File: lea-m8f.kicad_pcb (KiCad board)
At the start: 2 copper layers, 27 parts, among them CON1 USB-MICRO-B, J1 RF_IN, J2 DB9, J3 PPS, J4 30.72, P1 CONN_01X08, U100 B200_GPSDO, U2 MAX232, U3 LEA-M8F, U4 NC7SZ125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

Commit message: update pcb
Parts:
- removed C4: 100nF, SMD_Packages:SMD-0805
- removed C5: 10uF, SMD_Packages:SMD-0805
- removed C6: 10nF, SMD_Packages:SMD-0805
- removed C7: 1uF, SMD_Packages:SMD-0805
- removed J2: DB9, Connect:DB9FD
- removed U7: LT1962, lea-m8f:MS8
- added D1: DIODESCH, SMD_Packages:SMD-0603, F.Cu at (209.2, 66.9)
- added D2: PPS, SMD_Packages:SMD-0603, F.Cu at (197.9, 103.1)
- added D3: VDD, SMD_Packages:SMD-0603, F.Cu at (197.9, 109.7)
- added D4: DIODESCH, SMD_Packages:SMD-0603, B.Cu at (188.8, 97.4)
- added D5: VUSB, SMD_Packages:SMD-0603, F.Cu at (197.9, 106.4)
- added R10: 510, Resistors_SMD:R_0603_HandSoldering, F.Cu at (193.8, 103.1)
- added R11: 510, Resistors_SMD:R_0603_HandSoldering, F.Cu at (193.8, 109.7)
- added R12: 510, Resistors_SMD:R_0603_HandSoldering, F.Cu at (193.8, 106.4)
- added R8: 0, Resistors_SMD:R_0805, B.Cu at (195.5, 73.5)
- added U1: NC7SZ125, lea-m8f:SC70, F.Cu at (194.1, 99.3)
- C1: value 1uF -> 10uF
- C2: value 1uF -> 10nF
- U2: value MAX232 -> LT1962; footprint Housings_SOIC:SOIC-16_3.9x9.9mm_Pitch1.27mm -> lea-m8f:MS8
- moved C2 21.7 mm to (182.8, 99.0)
- moved C1 19.7 mm to (182.8, 96.7), turned to 180 degrees
- moved U2 18.7 mm to (183.8, 101.1), turned to 270 degrees
- moved C3 13.5 mm to (182.7, 107.9), turned to 180 degrees
- moved R1 2.69 mm to (195.5, 69.8), turned to 270 degrees
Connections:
- C1 pad 1: Net-(C1-Pad1) -> /VDDUSB
- C1 pad 2: Net-(C1-Pad2) -> GND
- C2 pad 2: Net-(C2-Pad2) -> /VDDUSB
- C3 pad 1: VCC -> /5VUSB
- C3 pad 2: Net-(C3-Pad2) -> GND
- P1 pad 1: (no net) -> VCC
- P1 pad 4: /SB_N -> /RESET_N
- P1 pad 5: (no net) -> /SCL
- P1 pad 6: /SCL -> /SDA
- P1 pad 7: /SDA -> /VBKP
- R1 pad 1: /ISP_N -> /SB_N
- R1 pad 2: /SB_N -> /ISP_N
- R6 pad 1: Net-(R6-Pad1) -> Net-(CON1-Pad3)
- R7 pad 1: Net-(R7-Pad1) -> Net-(CON1-Pad2)
- U100 pad 8: VCC -> /VDD_B200
- U2 pad 1: Net-(C1-Pad1) -> /VDDUSB
- U2 pad 2: Net-(C3-Pad2) -> /VDDUSB
- U2 pad 3: Net-(C1-Pad2) -> Net-(C2-Pad1)
- U2 pad 4: Net-(C2-Pad1) -> GND
- U2 pad 5: Net-(C2-Pad2) -> /5VUSB
- U2 pad 7: Net-(J2-Pad1) -> (no net)
- U2 pad 8: (no net) -> /5VUSB
- U3 pad 10: (no net) -> /RESET_N
- U3 pad 11: (no net) -> /VBKP
- U3 pad 24: VCC -> /VDDUSB
- U6 pad 6: Net-(R6-Pad1) -> Net-(CON1-Pad3)
- U6 pad 7: Net-(R7-Pad1) -> Net-(CON1-Pad2)
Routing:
- net VCC: track 149.1 -> 3.31 mm, vias 7 -> 2
- net /VBKP: track 0.00 -> 48.8 mm, vias 0 -> 1
- net /RESET_N: track 0.00 -> 47.9 mm, vias 0 -> 1
- net /VDDUSB: track 0.00 -> 46.6 mm, vias 0 -> 4
- net /SB_N: track 54.0 -> 18.3 mm, vias 3 -> 1
- net /PPS_BUFF: track 80.3 -> 56.7 mm
- net Net-(CON1-Pad2): track 6.08 -> 23.5 mm
- net Net-(CON1-Pad3): track 6.48 -> 23.6 mm
- net Net-(J2-Pad1): track 15.5 -> 0.00 mm
- net Net-(J2-Pad3): track 15.3 -> 0.00 mm, vias 1 -> 0
- net Net-(J2-Pad2): track 13.6 -> 0.00 mm, vias 1 -> 0
- net GND: track 115.3 -> 102.7 mm, vias 25 -> 34
- net /M8F_PPS: track 5.95 -> 18.1 mm, vias 0 -> 2
- net Net-(R7-Pad1): track 12.0 -> 0.00 mm
- net Net-(R6-Pad1): track 11.6 -> 0.00 mm
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- added copper zone on F.Cu, net VCC
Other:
- board text added: "1PPS"
- board text added: "VDD"
- board text added: "VUSB"
- board text added: "opendigitalradio.org"

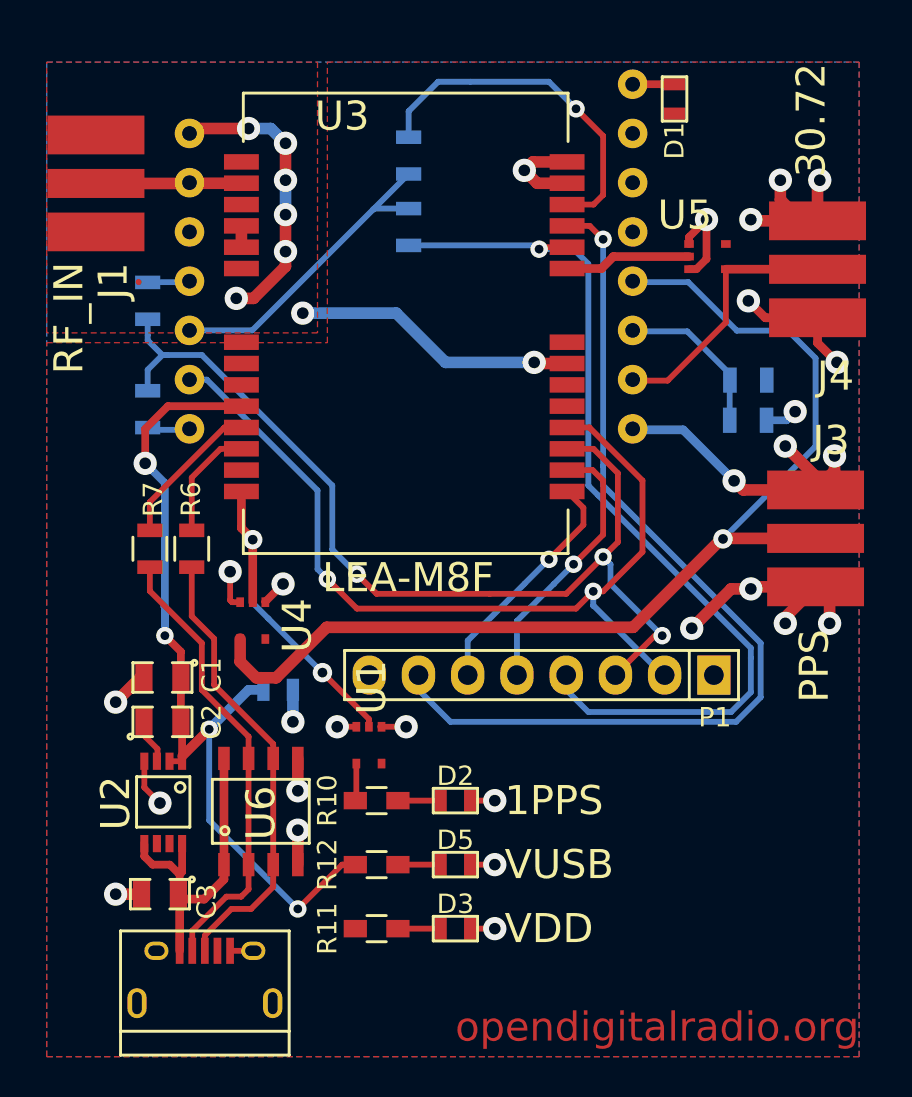
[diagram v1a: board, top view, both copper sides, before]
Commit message: Add text to PCB
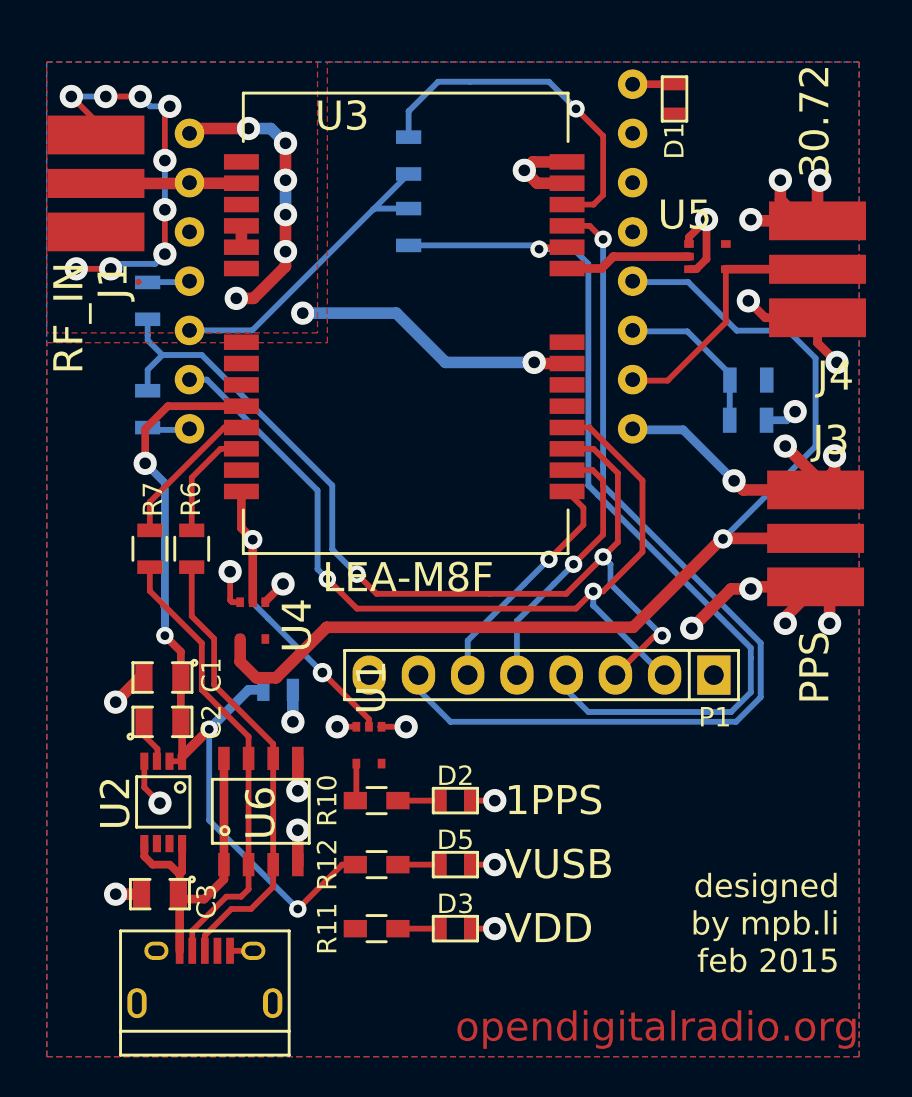
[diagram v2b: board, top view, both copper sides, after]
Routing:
- net GND: track 102.7 -> 123.2 mm, vias 34 -> 43
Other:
- board text added: "designed by mpb.li feb 2015"
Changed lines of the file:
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@@
     (links 95)
     (no_connects 0)
-    (area 0 0 0 0)
+    (area 175.646387 64.544615 219.2858 116.487901)
     (thickness 1.6)
-    (drawings 8)
-    (tracks 349)
+    (drawings 9)
+    (tracks 372)
     (zones 0)
     (modules 31)
@@
       (effects (font (size 1.5 1.5) (thickness 0.15)))
     )
-    (fp_text value PPS (at -0.0635 9.0805 90) (layer F.SilkS)
+    (fp_text value PPS (at -0.0381 9.1694 90) (layer F.SilkS)
       (effects (font (size 1.5 1.5) (thickness 0.15)))
     )
@@
       (effects (font (size 1.5 1.5) (thickness 0.15)))
     )
-    (fp_text value 30.72 (at -0.3302 -5.1943 90) (layer F.SilkS)
+    (fp_text value 30.72 (at -0.1397 -5.1435 90) (layer F.SilkS)
       (effects (font (size 1.5 1.5) (thickness 0.15)))
     )
@@
       (net 4 /5VUSB))
   )
+  (gr_text "designed\nby mpb.li\nfeb 2015" (at 217.7161 109.4359) (layer F.SilkS)
+    (effects (font (size 1.2 1.2) (thickness 0.2)) (justify right))
+  )
   (gr_line (start 176.8221 116.2939) (end 176.8221 64.9859) (angle 90) (layer Margin) (width 0.2))
   (gr_line (start 218.7321 116.2939) (end 176.8221 116.2939) (angle 90) (layer Margin) (width 0.2))
@@
   (via (at 215.4301 83.0199) (size 1.2) (layers F.Cu B.Cu) (net 2))
   (segment (start 214.9856 83.4644) (end 215.4301 83.0199) (width 0.4) (layer B.Cu) (net 2))
-  (segment (start 186.2801 110.8329) (end 187.4801 110.8329) (width 0.3) (layer F.Cu) (net 3) (status C00000))
+  (segment (start 179.3621 68.7489) (end 179.3621 68.0339) (width 0.3) (layer F.Cu) (net 3))
+  (segment (start 179.3621 68.0339) (end 178.0921 66.7639) (width 0.3) (layer F.Cu) (net 3))
+  (via (at 178.0921 66.7639) (size 1.2) (layers F.Cu B.Cu) (net 3))
+  (segment (start 178.0921 66.7639) (end 179.8701 66.7639) (width 0.3) (layer B.Cu) (net 3))
+  (via (at 179.8701 66.7639) (size 1.2) (layers F.Cu B.Cu) (net 3))
+  (segment (start 179.8701 66.7639) (end 181.6481 66.7639) (width 0.3) (layer F.Cu) (net 3))
+  (via (at 181.6481 66.7639) (size 1.2) (layers F.Cu B.Cu) (net 3))
+  (segment (start 181.6481 66.7639) (end 182.1561 67.2719) (width 0.3) (layer B.Cu) (net 3))
+  (segment (start 182.1561 67.2719) (end 183.1721 67.2719) (width 0.3) (layer B.Cu) (net 3))
+  (via (at 183.1721 67.2719) (size 1.2) (layers F.Cu B.Cu) (net 3))
+  (segment (start 183.1721 67.2719) (end 182.9181 67.5259) (width 0.3) (layer F.Cu) (net 3))
+  (segment (start 182.9181 67.5259) (end 182.9181 70.0659) (width 0.3) (layer F.Cu) (net 3))
+  (via (at 182.9181 70.0659) (size 1.2) (layers F.Cu B.Cu) (net 3))
+  (segment (start 182.9181 70.0659) (end 182.9181 72.6059) (width 0.3) (layer B.Cu) (net 3))
+  (via (at 182.9181 72.6059) (size 1.2) (layers F.Cu B.Cu) (net 3))
+  (segment (start 182.9181 72.6059) (end 182.9181 74.8919) (width 0.3) (layer F.Cu) (net 3))
+  (via (at 182.9181 74.8919) (size 1.2) (layers F.Cu B.Cu) (net 3))
+  (segment (start 182.9181 74.8919) (end 182.4101 75.3999) (width 0.3) (layer B.Cu) (net 3))
+  (segment (start 182.4101 75.3999) (end 180.3781 75.3999) (width 0.3) (layer B.Cu) (net 3))
+  (segment (start 180.3781 75.3999) (end 180.1241 75.6539) (width 0.3) (layer B.Cu) (net 3))
+  (via (at 180.1241 75.6539) (size 1.2) (layers F.Cu B.Cu) (net 3))
+  (segment (start 180.1241 75.6539) (end 178.3461 75.6539) (width 0.3) (layer F.Cu) (net 3))
+  (via (at 178.3461 75.6539) (size 1.2) (layers F.Cu B.Cu) (net 3))
+  (segment (start 186.2801 110.8329) (end 187.4801 110.8329) (width 0.3) (layer F.Cu) (net 3))
   (segment (start 198.6661 109.6899) (end 199.9361 109.6899) (width 0.3) (layer F.Cu) (net 3))
   (via (at 199.9361 109.6899) (size 1.2) (layers F.Cu B.Cu) (net 3))
@@
   )
   (zone (net 3) (net_name GND) (layer F.Cu) (hatch edge 0.508)
-    (connect_pads (clearance 0.3))
+    (connect_pads thru_hole_only (clearance 0.3))
     (min_thickness 0.254)
     (fill yes (arc_segments 16) (thermal_gap 0.4) (thermal_bridge_width 0.4))

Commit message: Correct LEA footprint, add silkscreen
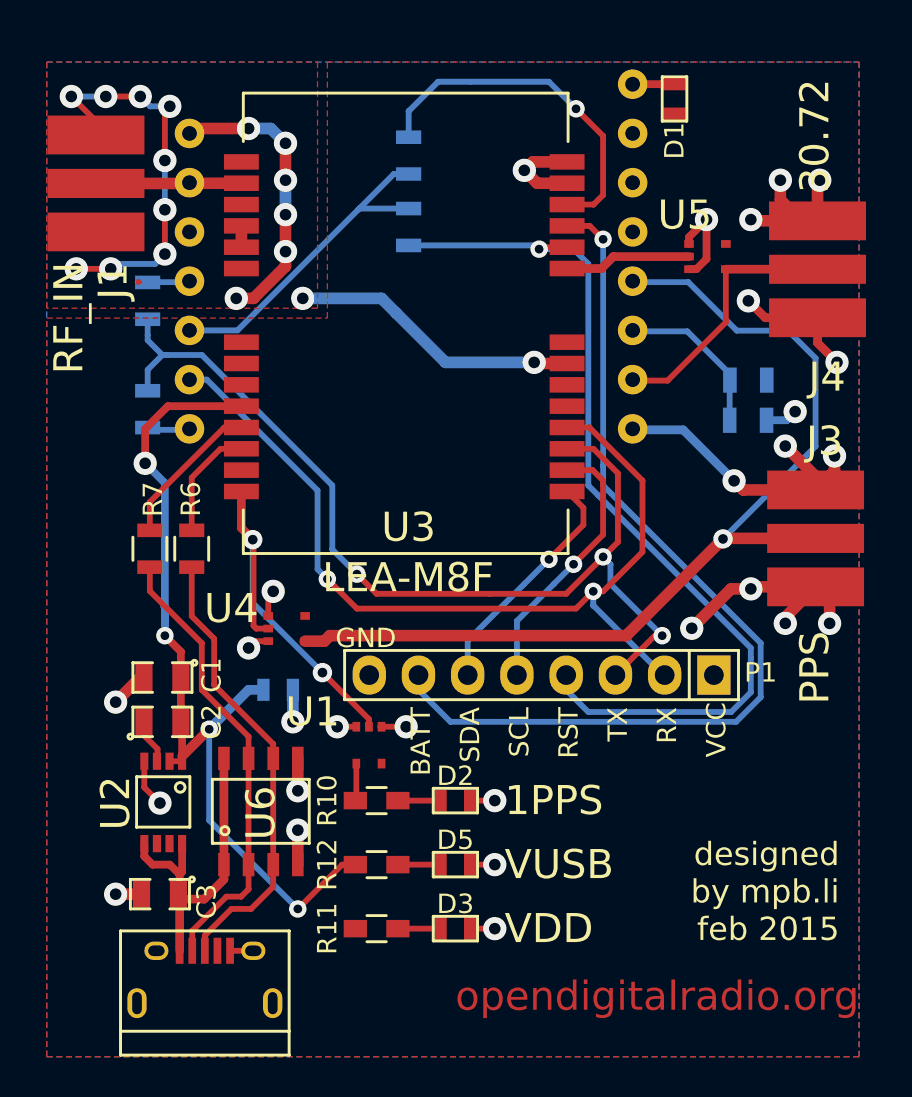
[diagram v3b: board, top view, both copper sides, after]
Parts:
- moved U4 0.73 mm to (188.3, 93.6), turned to 0 degrees
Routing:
- net /PPS_BUFF: track 56.7 -> 51.1 mm
- net /M8F_PPS: track 18.1 -> 20.2 mm
- net /ISP_N: track 17.2 -> 17.8 mm
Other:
- board text added: "BATT"
- board text added: "GND"
- board text added: "RST"
- board text added: "RX"
- board text added: "SCL"
- board text added: "SDA"
- board text added: "TX"
- board text added: "VCC"

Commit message: Fixed footprints and layout
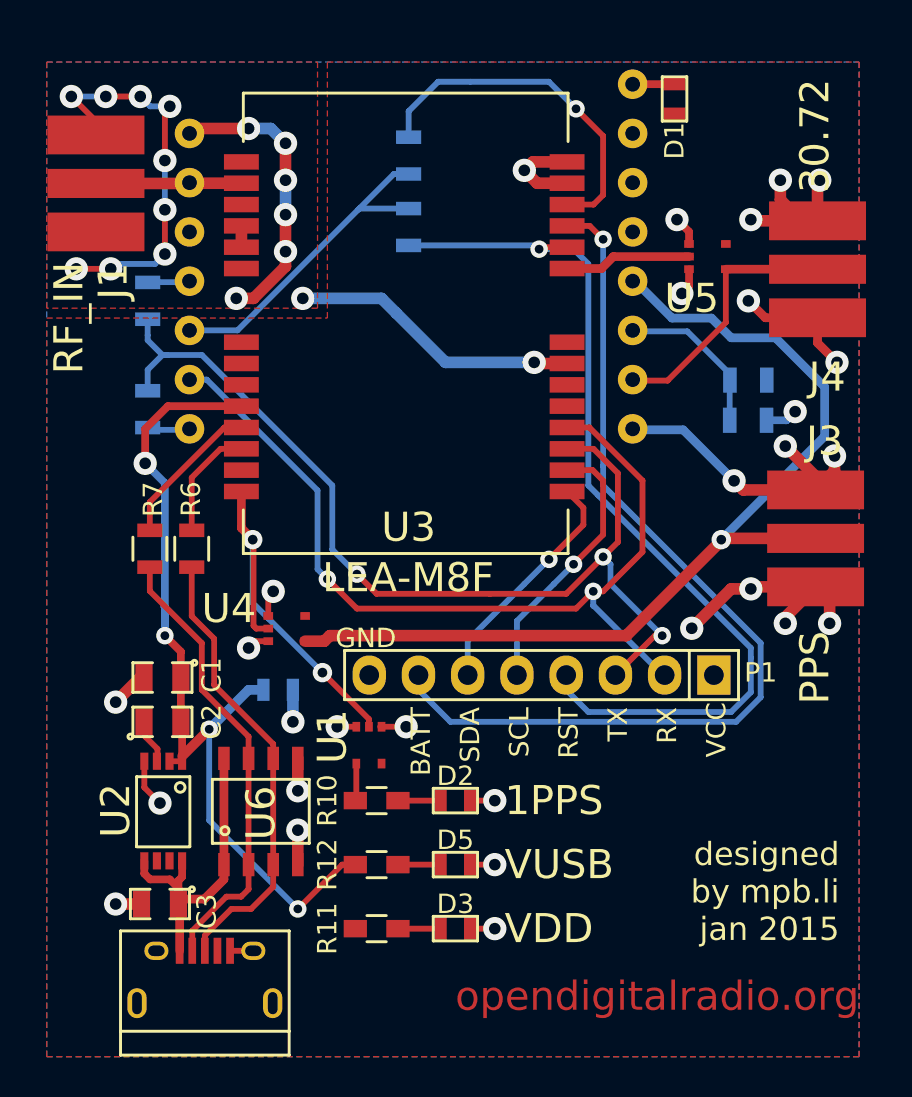
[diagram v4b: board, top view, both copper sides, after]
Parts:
- moved C3 0.51 mm to (182.7, 108.4)
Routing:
- net GND: track 122.7 -> 120.8 mm, vias 43 -> 44
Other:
- board text added: "designed by mpb.li jan 2015"
- board text removed: "designed by mpb.li feb 2015"

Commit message: Put GND below LEA
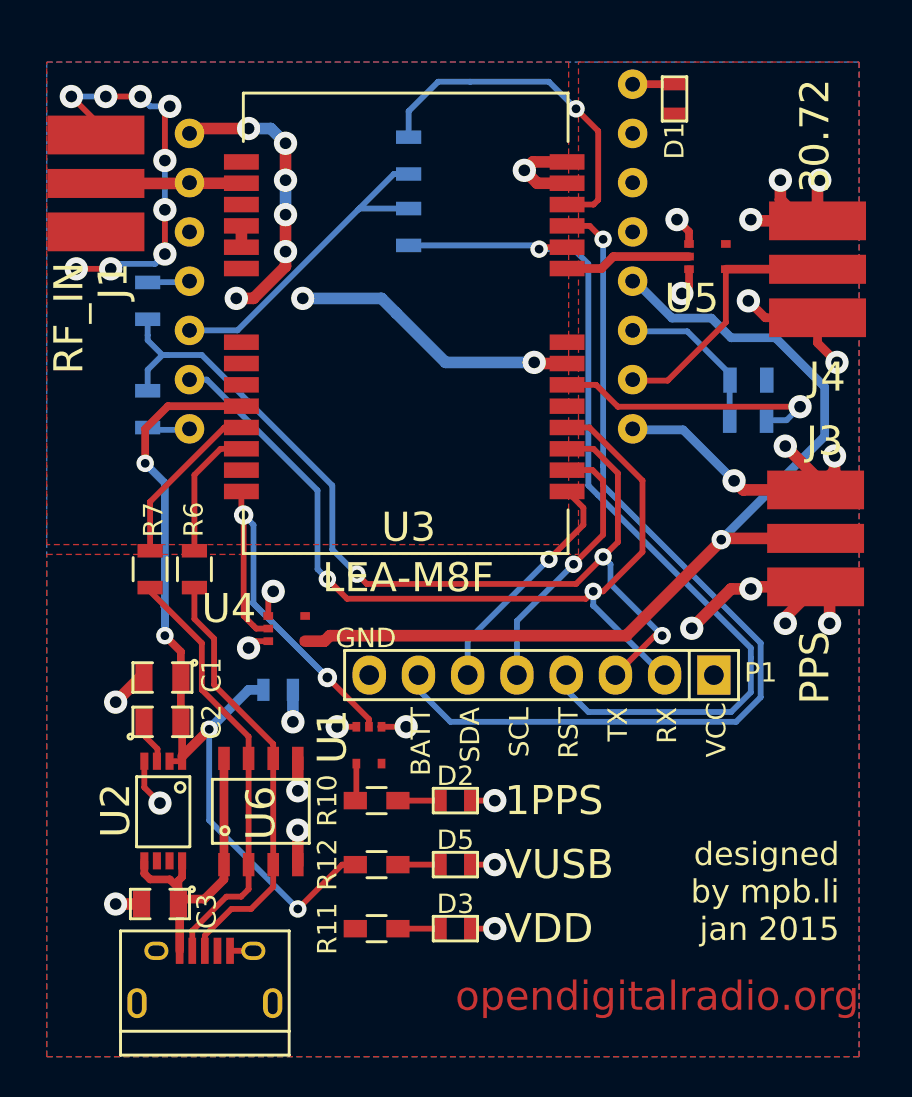
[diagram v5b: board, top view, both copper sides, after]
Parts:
- moved R6 1.06 mm to (184.4, 91.1)
- moved R7 1.05 mm to (182.2, 91.1)
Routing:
- net VCC: track 3.31 -> 16.2 mm
- net /M8F_PPS: track 20.2 -> 27.1 mm
- net Net-(CON1-Pad3): track 23.6 -> 22.5 mm
- net Net-(R7-Pad2): track 8.64 -> 9.73 mm
- net Net-(CON1-Pad2): track 23.5 -> 22.5 mm
- net Net-(R6-Pad2): track 5.90 -> 6.90 mm
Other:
- net class Power: via_drill 1 -> 0.8

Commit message: Update footprints
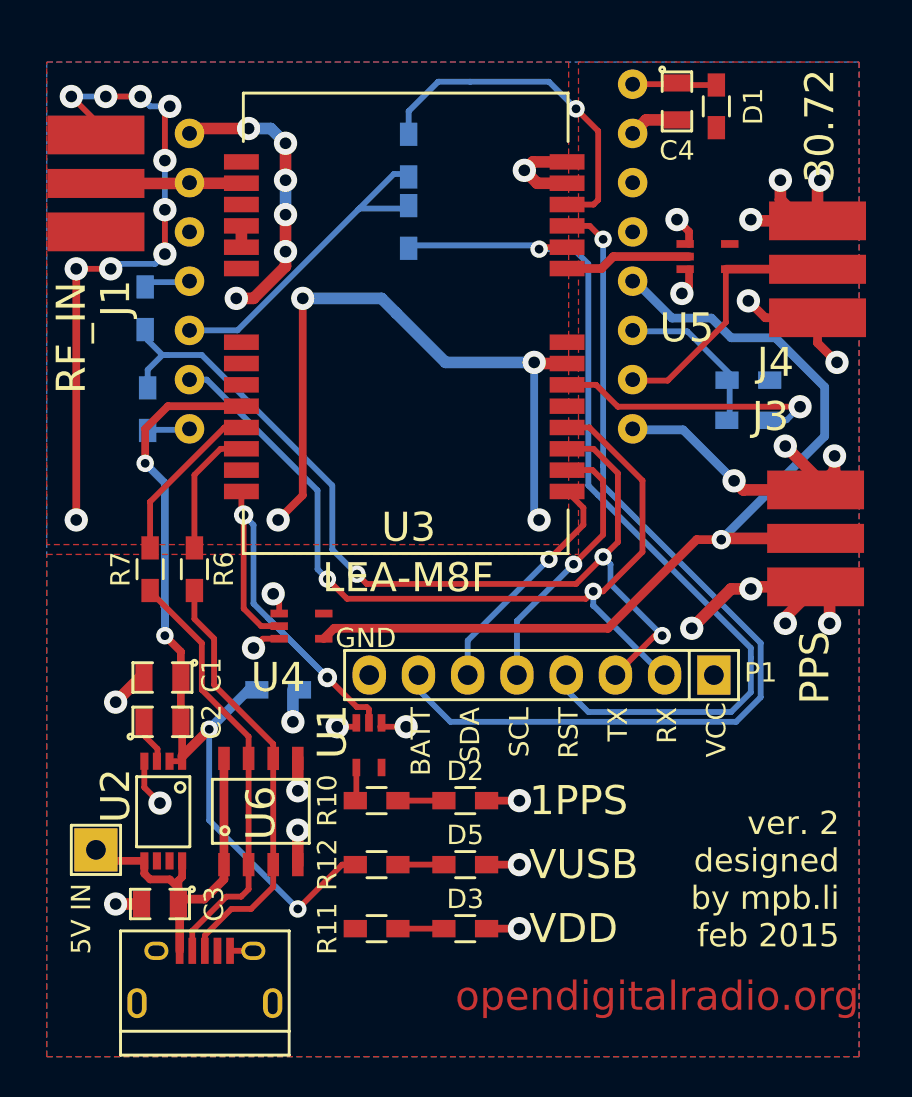
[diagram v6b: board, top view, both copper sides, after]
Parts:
- added C4: 1uF, SMD_Packages:SMD-0805, F.Cu at (209.3, 67.0)
- added P2: 5V IN, Pin_Headers:Pin_Header_Straight_1x01, F.Cu at (179.4, 105.6)
- D1, D2, D3, D4, D5: footprint SMD_Packages:SMD-0603 -> Resistors_SMD:R_0603_HandSoldering
- R1, R5, R8: value 0 -> DNF; footprint Resistors_SMD:R_0805 -> Resistors_SMD:R_0603_HandSoldering
- R2, R3, R4, R6, R7: footprint Resistors_SMD:R_0805 -> Resistors_SMD:R_0603_HandSoldering
- moved D1 2.19 mm to (211.4, 67.3)
- moved U4 0.77 mm to (189.0, 93.4)
- moved D2 0.51 mm to (198.4, 103.1)
- moved D3 0.51 mm to (198.4, 109.7)
- moved D5 0.51 mm to (198.4, 106.4)
- moved R3 0.40 mm to (181.9, 77.7)
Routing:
- net GND: track 120.8 -> 157.9 mm, vias 44 -> 47
- net /5VUSB: track 17.4 -> 20.2 mm
- net /VDD_B200: track 2.16 -> 4.39 mm
- net /PPS_BUFF: track 51.0 -> 49.9 mm
- net /TXD: track 50.9 -> 50.1 mm
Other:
- board text added: "ver. 2 designed by mpb.li feb 2015"
- board text removed: "designed by mpb.li jan 2015"
